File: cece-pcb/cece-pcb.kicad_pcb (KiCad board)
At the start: 2 copper layers, 57 x 80.5 mm, 41 parts, among them J101 VAC, J102 HTU21D, J103 SERIAL, J104 Li-Ion Battery, K101 SANYOU_SRD_Form_C, Q101 Q_NPN, SW201 RES, U101 TLV75533PDBV, U102 MCP73811T-420I-OT, U201 ESP-12F

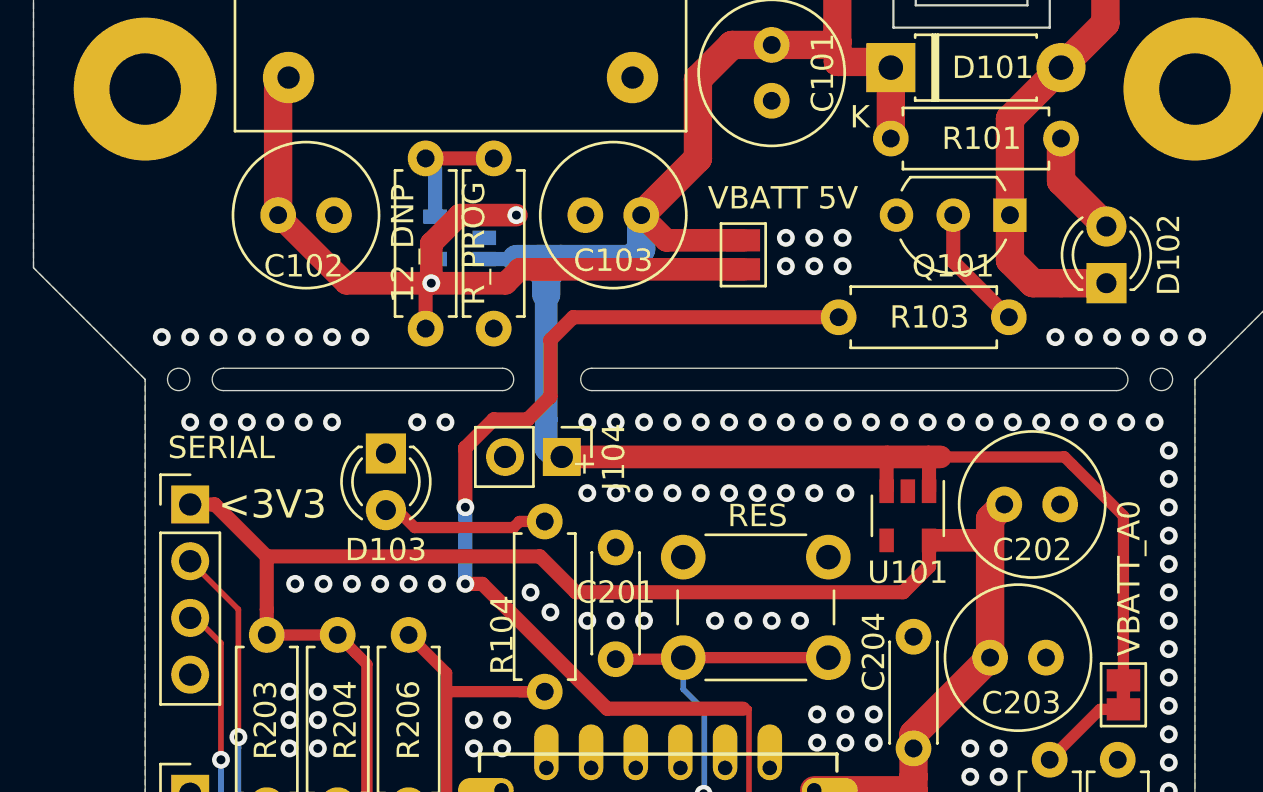
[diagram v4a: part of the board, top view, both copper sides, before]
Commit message: Add diode to protect the seral input when 3V3 are already supplied internally and shuffle stuff around a bit on the layout
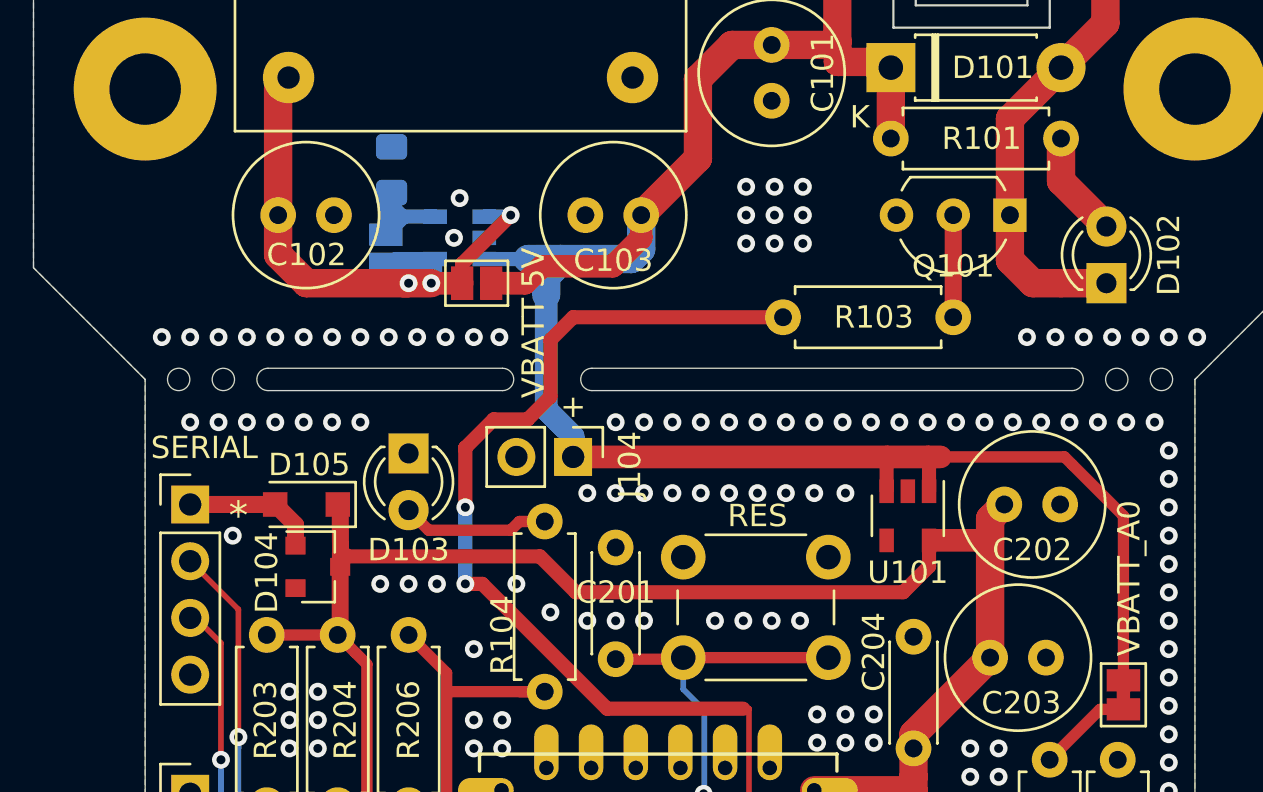
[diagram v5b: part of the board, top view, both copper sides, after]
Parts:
- removed R102: 12_DNP, Resistor_THT:R_Axial_DIN0207_L6.3mm_D2.5mm_P7.62mm_Horizontal
- added D104: Schottky SOT-23, Diode_SMD:D_SOT-23_ANK, F.Cu at (125.7, 88.4)
- added D105: Schottky SOD-123, Diode_SMD:D_SOD-123F, F.Cu at (125.2, 85.6)
- added JP103: 73811, Jumper:SolderJumper-2_P1.3mm_Open_Pad1.0x1.5mm, B.Cu at (128.8, 74.2)
- R105: footprint Resistor_THT:R_Axial_DIN0207_L6.3mm_D2.5mm_P7.62mm_Horizontal -> Resistor_SMD:R_0805_2012Metric_Pad1.15x1.40mm_HandSolder; moved to B.Cu
- moved JP102 12.0 mm to (132.8, 75.7), turned to 0 degrees
- moved R105 4.60 mm to (129.0, 70.6), turned to 90 degrees
- moved R103 2.49 mm to (154.2, 77.2)
- moved D103 1.02 mm to (129.8, 83.3)
- moved J104 0.51 mm to (137.2, 83.5)
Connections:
- J103 pad 1: +3V3 -> Net-(D104-Pad2)
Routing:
- net +5V: track 39.9 -> 32.3 mm, vias 2 -> 3
- net Net-(D104-Pad2): track 0.00 -> 6.03 mm
- net +3V3: track 80.9 -> 75.5 mm
- net /RLY: track 50.1 -> 47.6 mm
- net Net-(D103-Pad2): track 7.76 -> 6.63 mm
- net Net-(Q101-Pad2): track 5.60 -> 4.57 mm
- net +BATT: track 90.8 -> 91.6 mm
- net GND: vias 172 -> 180
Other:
- outline, holes or cut-outs redrawn
- board text added: "*"
